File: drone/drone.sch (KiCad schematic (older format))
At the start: 32 parts, among them IC1 AT89S4051-P, P1 LeftM, P2 ISP, P3 RightM, P4 Blade1, P5 Blade2, Q1 NPN, Q2 PNP, Q3 NPN, Q4 PNP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

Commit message: Fix the circuit
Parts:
- removed P3: RightM, symbol CONN_2
- removed Q2, Q4, Q6, Q8: PNP, symbol PNP
- removed Q5: NPN, symbol NPN
- removed R5: 1K, symbol R
- added P5: RightM, symbol CONN_2
- added Q2, Q4, Q6, Q8, Q9: NPN, symbol NPN
- added R9: 1K, symbol R
- renumbered P4 to P3, P5 to P4, Q9 to Q5, R9 to R5
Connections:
- wire segments 92 -> 94

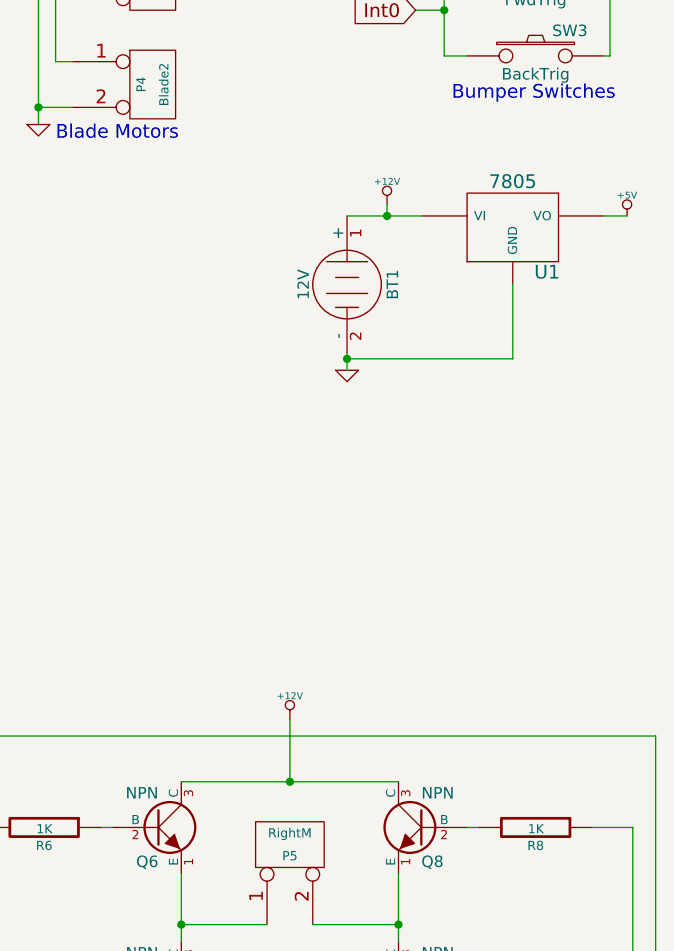
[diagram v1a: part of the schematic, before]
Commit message: Fixed design rules check fail
* It just needed such a pwr-flag on the power and ground networks
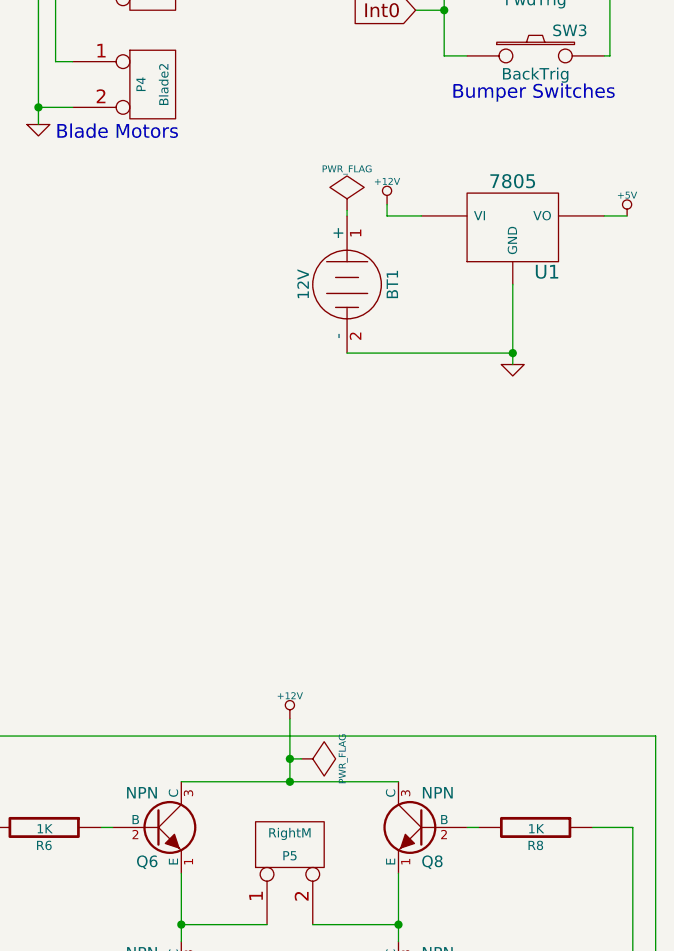
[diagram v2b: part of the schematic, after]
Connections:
- net +12V: no longer BT1.1 (+)
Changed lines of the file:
@@
 $EndComp
-$Comp
-L GND #PWR011
-U 1 1 556F30B9
-P 8400 2975
-F 0 "#PWR011" H 8400 2975 30  0001 C CNN
-F 1 "GND" H 8400 2905 30  0001 C CNN
-F 2 "" H 8400 2975 60  0000 C CNN
-F 3 "" H 8400 2975 60  0000 C CNN
-	1    8400 2975
-	1    0    0    -1
-$EndComp
-Wire Wire Line
-	8400 2900 8400 2975
 $Comp
 L 7805 U1
@@
 $EndComp
 Wire Wire Line
-	8400 2300 8725 2300
-Connection ~ 8575 2300
-Wire Wire Line
 	9525 2300 9625 2300
 Wire Wire Line
-	9125 2600 9125 2925
-Wire Wire Line
-	9125 2925 8400 2925
-Connection ~ 8400 2925
+	9125 2600 9125 2950
 NoConn ~ 2925 50
 Text GLabel 1700 4750 0    60   Input ~ 0
@@
 	4275 1775 4350 1775
 $Comp
-L +12V #PWR012
+L +12V #PWR011
 U 1 1 556F6D84
 P 7125 625
-F 0 "#PWR012" H 7125 575 20  0001 C CNN
+F 0 "#PWR011" H 7125 575 20  0001 C CNN
 F 1 "+12V" H 7125 725 30  0000 C CNN
 F 2 "" H 7125 625 60  0000 C CNN
@@
 	7325 4975 7375 4975
 $Comp
-L +12V #PWR013
+L +12V #PWR012
 U 1 1 55708FC2
 P 3475 4325
-F 0 "#PWR013" H 3475 4275 20  0001 C CNN
+F 0 "#PWR012" H 3475 4275 20  0001 C CNN
 F 1 "+12V" H 3475 4425 30  0000 C CNN
 F 2 "" H 3475 4325 60  0000 C CNN
@@
 Connection ~ 3475 4600
 $Comp
-L GND #PWR014
+L GND #PWR013
 U 1 1 55709044
 P 3475 5750
-F 0 "#PWR014" H 3475 5750 30  0001 C CNN
+F 0 "#PWR013" H 3475 5750 30  0001 C CNN
 F 1 "GND" H 3475 5680 30  0001 C CNN
 F 2 "" H 3475 5750 60  0000 C CNN
@@
 Connection ~ 3475 5700
 $Comp
-L +12V #PWR015
+L +12V #PWR014
 U 1 1 557090C8
 P 8150 4500
-F 0 "#PWR015" H 8150 4450 20  0001 C CNN
+F 0 "#PWR014" H 8150 4450 20  0001 C CNN
 F 1 "+12V" H 8150 4600 30  0000 C CNN
 F 2 "" H 8150 4500 60  0000 C CNN
@@
 $EndComp
 $Comp
-L GND #PWR016
+L GND #PWR015
 U 1 1 557090DC
 P 8150 5975
-F 0 "#PWR016" H 8150 5975 30  0001 C CNN
+F 0 "#PWR015" H 8150 5975 30  0001 C CNN
 F 1 "GND" H 8150 5905 30  0001 C CNN
 F 2 "" H 8150 5975 60  0000 C CNN
@@
 Connection ~ 8150 4775
 Wire Wire Line
-	8575 2300 8575 2250
-Wire Wire Line
-	8150 4775 8150 4500
+	8150 4500 8150 4775
+$Comp
+L PWR_FLAG #FLG016
+U 1 1 5570B235
+P 8400 2275
+F 0 "#FLG016" H 8400 2370 30  0001 C CNN
+F 1 "PWR_FLAG" H 8400 2455 30  0000 C CNN
+F 2 "" H 8400 2275 60  0000 C CNN
+F 3 "" H 8400 2275 60  0000 C CNN
+	1    8400 2275
+	1    0    0    -1
+$EndComp
+Wire Wire Line
+	8400 2300 8400 2275
+Wire Wire Line
+	8575 2250 8575 2300
+Wire Wire Line
+	8575 2300 8725 2300
+$Comp
+L GND #PWR017
+U 1 1 5570B423
+P 9125 2950
+F 0 "#PWR017" H 9125 2950 30  0001 C CNN
+F 1 "GND" H 9125 2880 30  0001 C CNN
+F 2 "" H 9125 2950 60  0000 C CNN
+F 3 "" H 9125 2950 60  0000 C CNN
+	1    9125 2950
+	1    0    0    -1
+$EndComp
+$Comp
+L PWR_FLAG #FLG018
+U 1 1 5570B4AC
+P 8200 4675
+F 0 "#FLG018" H 8200 4770 30  0001 C CNN
+F 1 "PWR_FLAG" H 8200 4855 30  0000 C CNN
+F 2 "" H 8200 4675 60  0000 C CNN
+F 3 "" H 8200 4675 60  0000 C CNN
+	1    8200 4675
+	0    1    1    0
+$EndComp
+Wire Wire Line
+	8200 4675 8150 4675
+Connection ~ 8150 4675
+Wire Wire Line
+	8400 2900 9125 2900
+Connection ~ 9125 2900
 $EndSCHEMATC

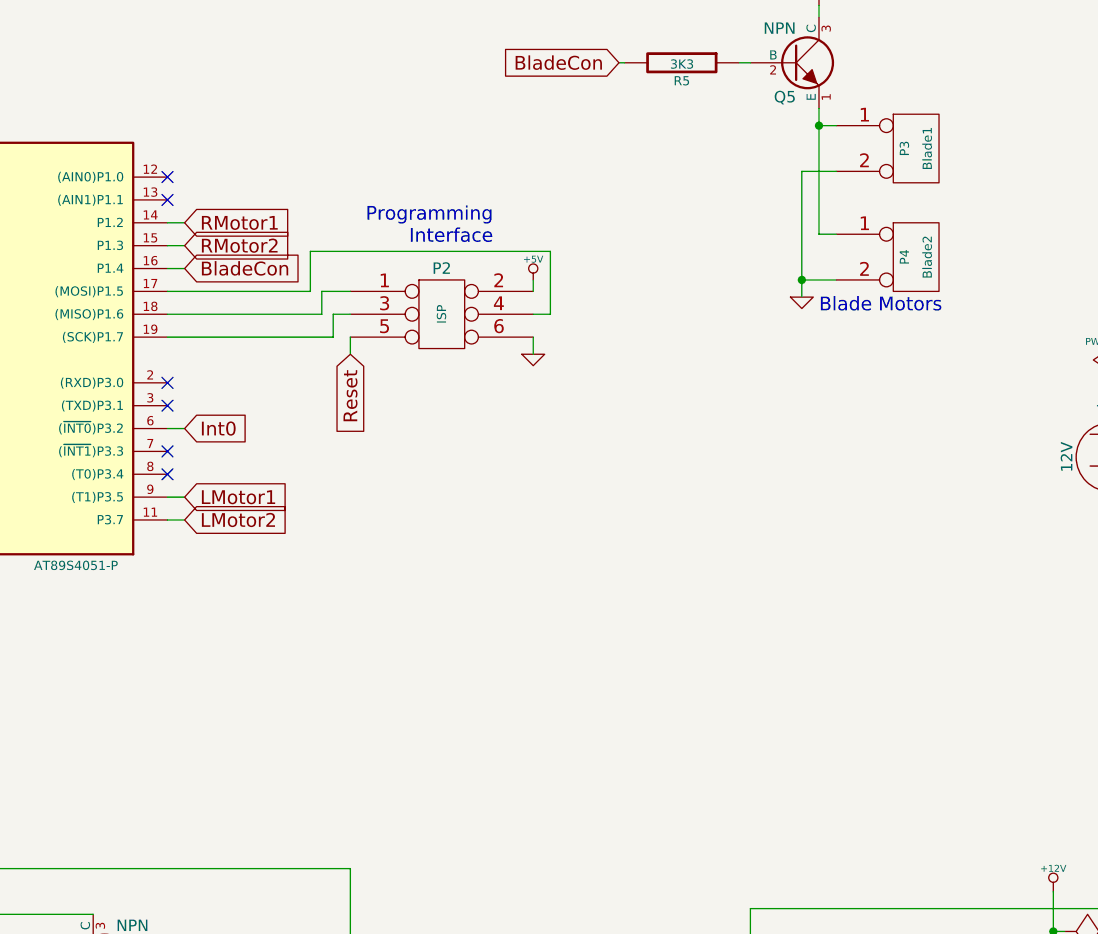
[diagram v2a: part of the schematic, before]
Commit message: Added ultrasonic range finder to schematic
* Added an ultra sonic rangefinder to schematic

Avail Here: http://www.amazon.com/SunFounder-Ultrasonic-Distance-Mega2560-Duemilanove/dp/B00E0NXTJW/ref=sr_1_1?ie=UTF8&qid=1433724748&sr=8-1&keywords=Ultrasonic+arduino
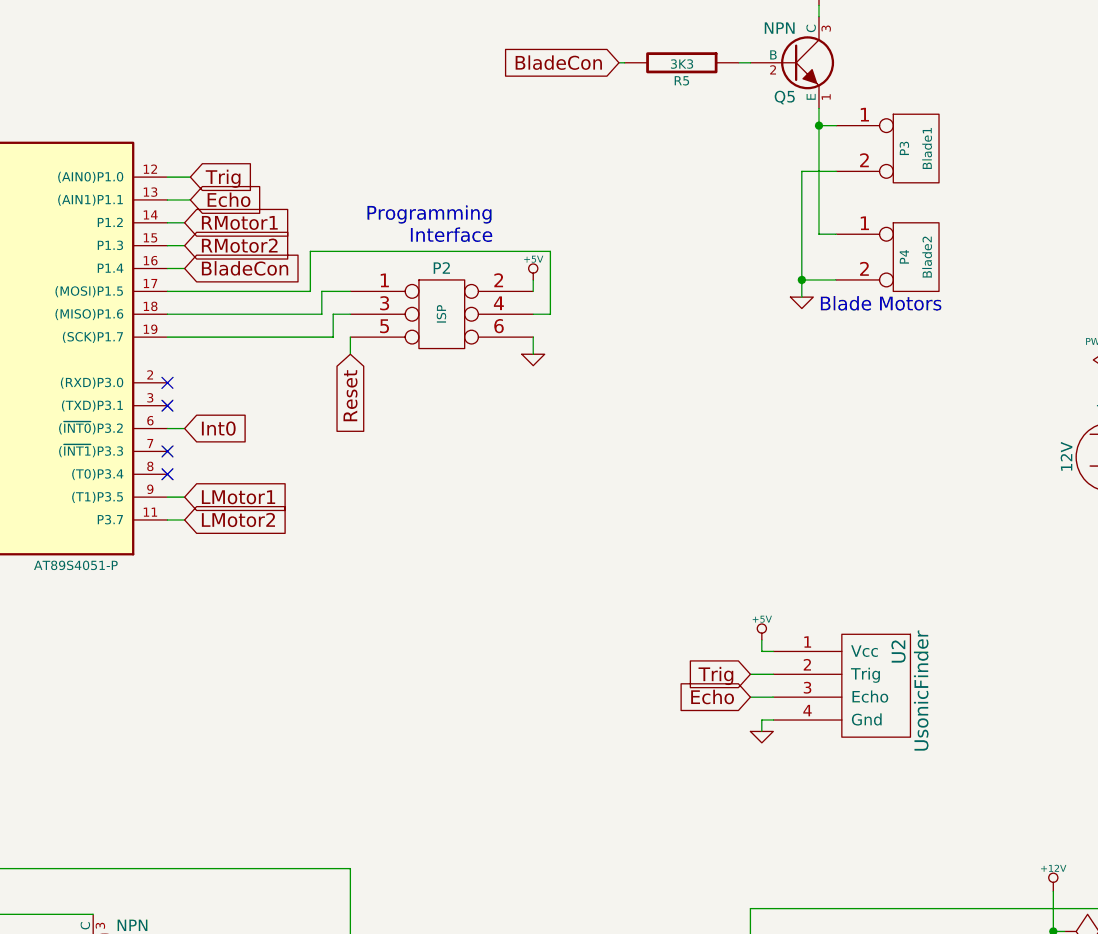
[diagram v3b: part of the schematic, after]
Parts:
- added U2: UsonicFinder, symbol UsonicFinder
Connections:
- net +5V: now also U2.1 (Vcc)
- net GND: now also U2.4 (Gnd)
- net Trig: now reaches IC1.12 ((AIN0)P1.0)
- net Trig: now also U2.2 (Trig)
- net Echo: now reaches IC1.13 ((AIN1)P1.1)
- net Echo: now also U2.3 (Echo)
- no-connect marks 7 -> 5
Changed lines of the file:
@@
 Wire Wire Line
 	4275 1675 4350 1675
-NoConn ~ 4275 1475
-NoConn ~ 4275 1375
 NoConn ~ 4275 2375
 NoConn ~ 4275 2675
@@
 	8400 2900 9125 2900
 Connection ~ 9125 2900
+$Comp
+L UsonicFinder U2
+U 1 1 5574E94F
+P 7225 3600
+F 0 "U2" H 7075 3850 60  0000 C CNN
+F 1 "UsonicFinder" H 7250 3950 60  0000 C CNN
+F 2 "" H 7225 3600 60  0000 C CNN
+F 3 "" H 7225 3600 60  0000 C CNN
+	1    7225 3600
+	0    1    1    0
+$EndComp
+$Comp
+L +5V #PWR019
+U 1 1 5574E963
+P 6875 3400
+F 0 "#PWR019" H 6875 3490 20  0001 C CNN
+F 1 "+5V" H 6875 3490 30  0000 C CNN
+F 2 "" H 6875 3400 60  0000 C CNN
+F 3 "" H 6875 3400 60  0000 C CNN
+	1    6875 3400
+	1    0    0    -1
+$EndComp
+Wire Wire Line
+	6875 3400 6875 3450
+Wire Wire Line
+	6875 3450 6925 3450
+$Comp
+L GND #PWR020
+U 1 1 5574EA64
+P 6875 3800
+F 0 "#PWR020" H 6875 3800 30  0001 C CNN
+F 1 "GND" H 6875 3730 30  0001 C CNN
+F 2 "" H 6875 3800 60  0000 C CNN
+F 3 "" H 6875 3800 60  0000 C CNN
+	1    6875 3800
+	1    0    0    -1
+$EndComp
+Wire Wire Line
+	6875 3800 6875 3750
+Wire Wire Line
+	6875 3750 6925 3750
+Text GLabel 4375 1375 2    60   Input ~ 0
+Trig
+Wire Wire Line
+	4275 1375 4375 1375
+Text GLabel 4375 1475 2    60   Input ~ 0
+Echo
+Wire Wire Line
+	4275 1475 4375 1475
+Text GLabel 6825 3550 0    60   Input ~ 0
+Trig
+Text GLabel 6825 3650 0    60   Input ~ 0
+Echo
+Wire Wire Line
+	6825 3650 6925 3650
+Wire Wire Line
+	6925 3550 6825 3550
 $EndSCHEMATC
